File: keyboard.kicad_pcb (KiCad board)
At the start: 2 copper layers, 30 parts, among them J1 CONN-PALM-FOLD-KB, P1 CONN_25, P2 CONN_25, P3 PS2, P4 CONN_6, U1 CONN-X220-KB

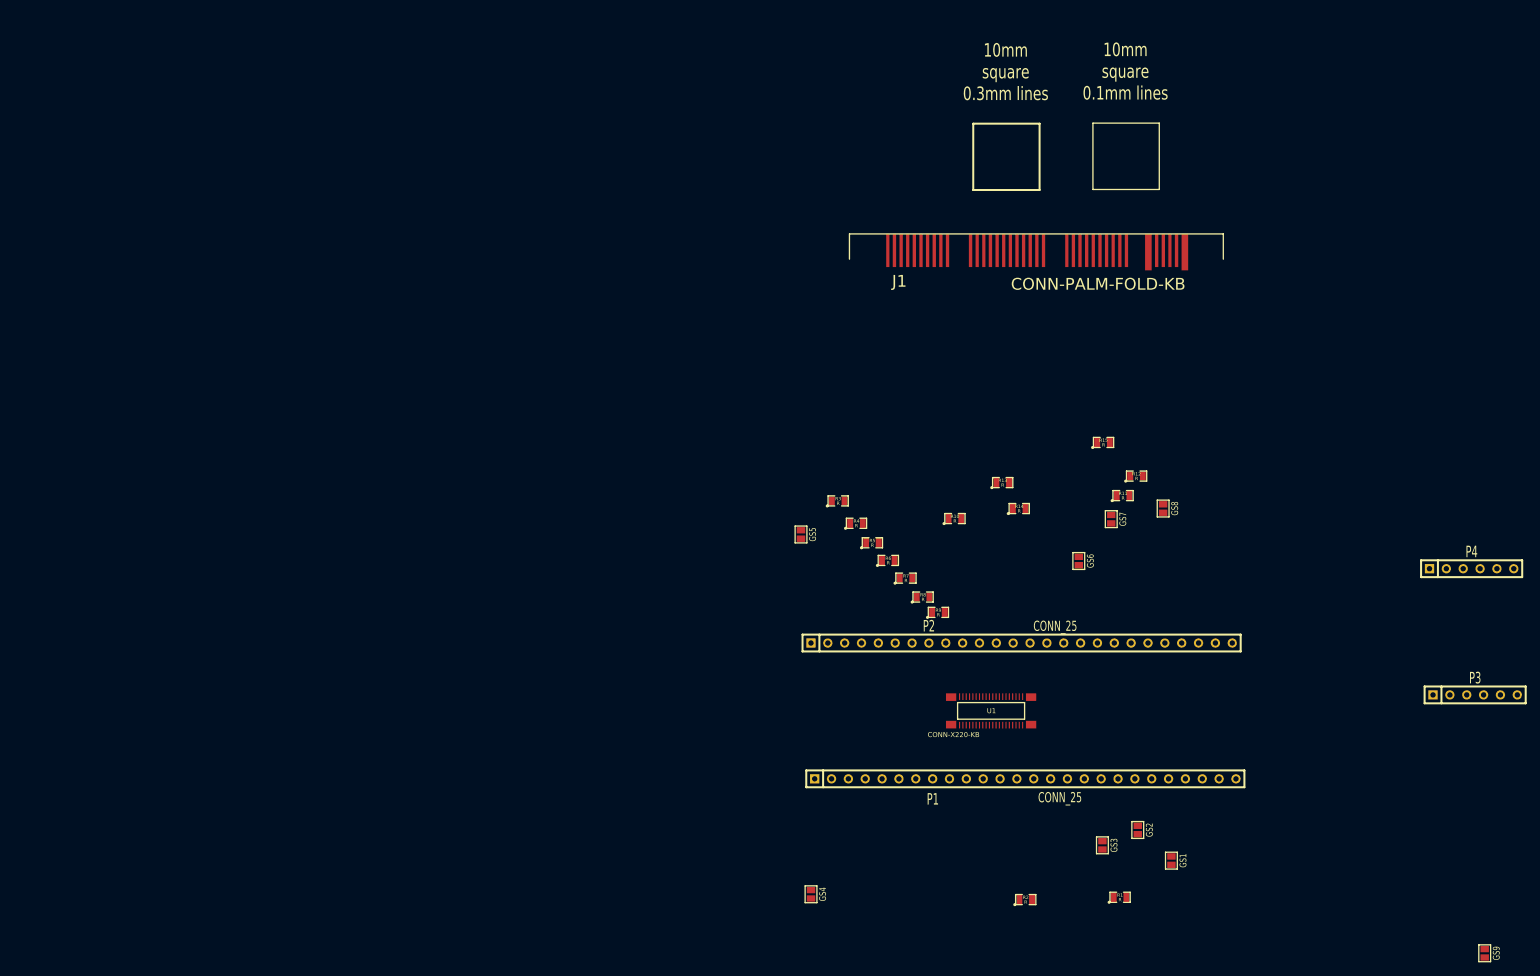
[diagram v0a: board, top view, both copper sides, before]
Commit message: Import all components into PCB
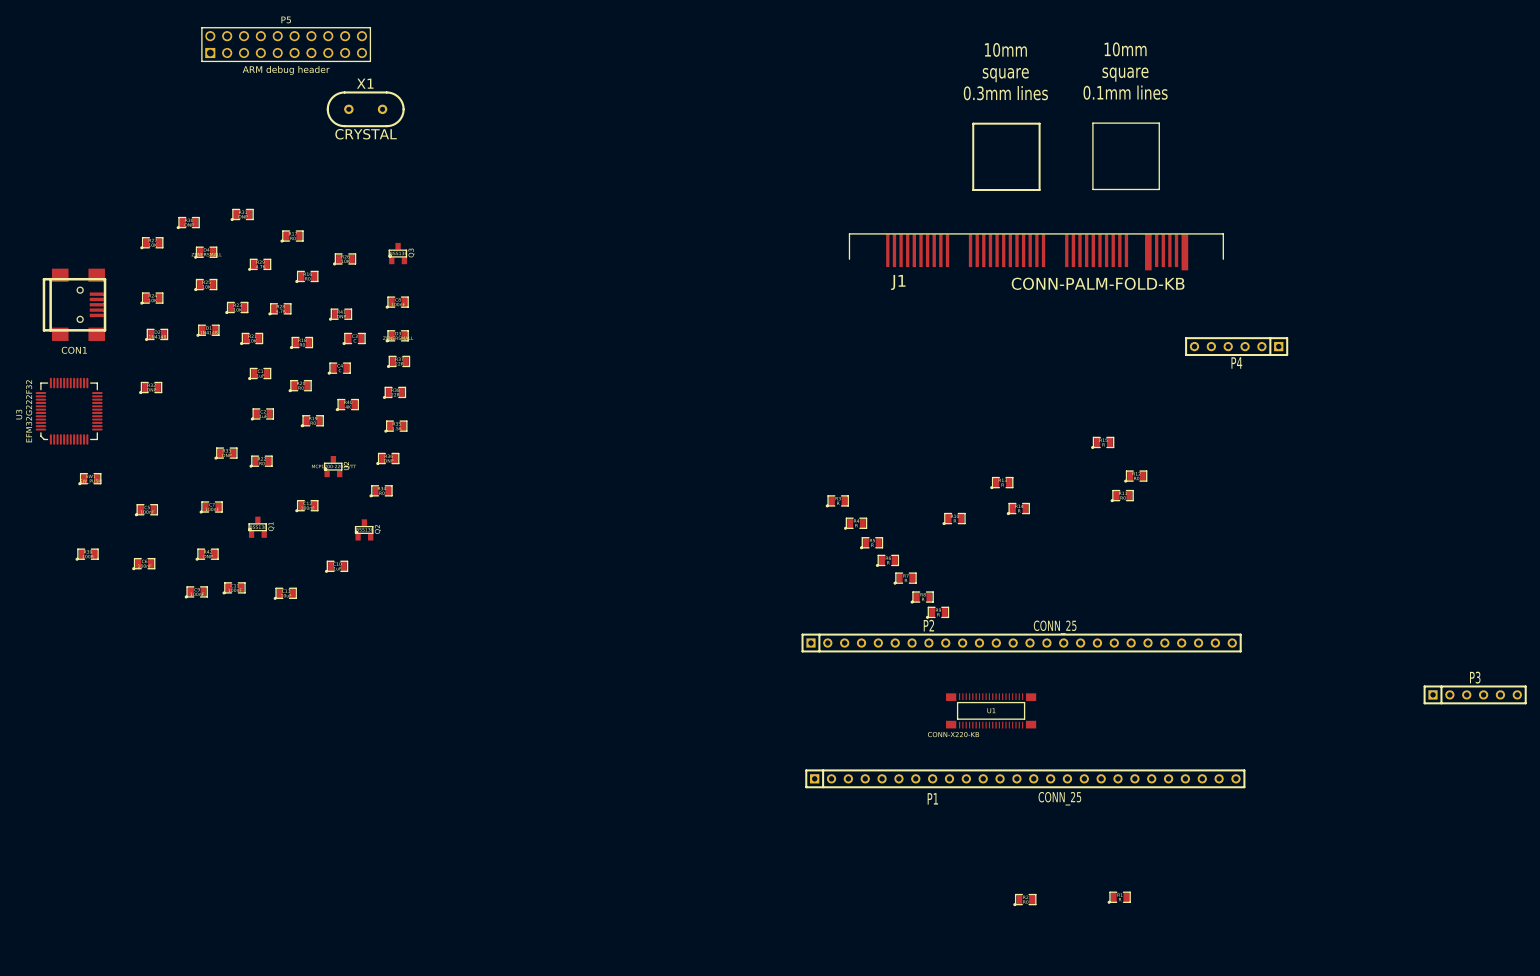
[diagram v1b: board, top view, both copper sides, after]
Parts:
- removed GS1, GS2, GS3, GS4, GS5, GS6, GS7, GS8, GS9: GS2, GS2
- added C1: 1uF, SM0805, F.Cu at (49.6, 67.7)
- added C10: 1uF, SM0805, F.Cu at (61.2, 96.7)
- added C11: 100nF, SM0805, F.Cu at (45.7, 100.0)
- added C12: 100nF, SM0805, F.Cu at (56.7, 87.6)
- added C13: 10uF, SM0805, F.Cu at (53.4, 100.8)
- added C2: 1uF, SM0805, F.Cu at (50.0, 73.8)
- added C3: C, SM0805, F.Cu at (63.8, 62.4)
- added C4: C, SM0805, F.Cu at (61.6, 66.8)
- added C5: 100nF, SM0805, F.Cu at (32.5, 88.2)
- added C6: 100nF, SM0805, F.Cu at (32.1, 96.3)
- added C7: 100nF, SM0805, F.Cu at (42.3, 87.8)
- added C8: 100nF, SM0805, F.Cu at (70.3, 56.9)
- added C9: 100nF, SM0805, F.Cu at (40.0, 100.6)
- added CON1: USB-MICRO-B, USB_MINI_B, F.Cu at (21.5, 57.3)
- added D1: 1N4148, SM0805, F.Cu at (41.8, 61.1)
- added D2: 1N4148, SM0805, F.Cu at (34.0, 61.8)
- added D3: ZENERSMALL, SM0805, F.Cu at (70.3, 62.0)
- added D4: ZENERSMALL, SM0805, F.Cu at (41.5, 49.4)
- added P5: ARM debug header, pin_array_10x2, F.Cu at (53.4, 18.1)
- added Q1: BSS138, SOT23, F.Cu at (49.2, 90.8)
- added Q2: BSS138, SOT23, F.Cu at (65.2, 91.2)
- added Q3: BSS138, SOT23, F.Cu at (70.3, 49.6)
- added R16: R0, SM0805, F.Cu at (56.7, 53.0)
- added R17: R0, SM0805, F.Cu at (54.5, 46.9)
- added R18: R0, SM0805, F.Cu at (55.9, 63.0)
- added R19: R0, SM0805, F.Cu at (57.5, 74.8)
- added R20: R0, SM0805, F.Cu at (55.7, 69.5)
- added R21: 10K, SM0805, F.Cu at (48.4, 62.4)
- added R22: R0, SM0805, F.Cu at (49.8, 80.9)
- added R23: 10K, SM0805, F.Cu at (46.1, 57.7)
- added R24: 10K, SM0805, F.Cu at (33.3, 56.3)
- added R25: 10K, SM0805, F.Cu at (41.5, 54.2)
- added R26: 10K, SM0805, F.Cu at (62.4, 50.4)
- added R27: 10K, SM0805, F.Cu at (33.3, 48.0)
- added R28: 4.7K, SM0805, F.Cu at (52.6, 57.9)
- added R29: 4.7K, SM0805, F.Cu at (49.6, 51.2)
- added R30: DNP, SM0805, F.Cu at (38.8, 44.9)
- added R31: DNP, SM0805, F.Cu at (46.9, 43.7)
- added R32: DNP, SM0805, F.Cu at (33.1, 69.8)
- added R33: DNP, SM0805, F.Cu at (44.5, 79.7)
- added R34: R0, SM0805, F.Cu at (67.9, 85.3)
- added R35: 1.5K, SM0805, F.Cu at (70.1, 75.6)
- added R36: DNP, SM0805, F.Cu at (68.9, 80.5)
- added R37: 22R, SM0805, F.Cu at (70.5, 65.8)
- added R38: 22R, SM0805, F.Cu at (69.9, 70.5)
- added R39: 100R, SM0805, F.Cu at (23.6, 94.9)
- added R40: 4K, SM0805, F.Cu at (62.8, 72.3)
- added R41: DNP, SM0805, F.Cu at (61.8, 58.7)
- added R42: DNP, SM0805, F.Cu at (41.7, 94.9)
- added SW1: SW_PUSH, SM0805, F.Cu at (24.0, 83.5)
- added U2: MCP1700-2202E/TT, SOT23, F.Cu at (60.6, 81.7)
- added U3: EFM32G222F32, EFM32_TQFP48, F.Cu at (20.7, 73.3)
- added X1: CRYSTAL, HC-49V, F.Cu at (65.4, 27.8)
- R11, R12, R2: value R -> R0
- moved P4 48.7 mm to (196.7, 63.6), turned to 180 degrees
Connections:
- P1 pad 18: N-0000020 (its old number) -> N-0000057
- P1 pad 20: N-0000018 (its old number) -> N-0000055
- P1 pad 22: N-0000016 (its old number) -> N-0000053
- R11 pad 2: tp4data -> N-0000055
- R12 pad 1: +5V -> GND
- R12 pad 2: tp4_clk -> N-0000057
- R13 pad 2: (no net) -> ledcpslock
- R14 pad 2: (no net) -> ledpwr
- R15 pad 2: (no net) -> led_mute
- R2 pad 1: +5V -> GND
- R2 pad 2: tp4_reset -> N-0000053
- U1 pad 34: N-0000020 (its old number) -> N-0000057
- U1 pad 38: N-0000018 (its old number) -> N-0000055
- U1 pad 44: N-0000016 (its old number) -> N-0000053

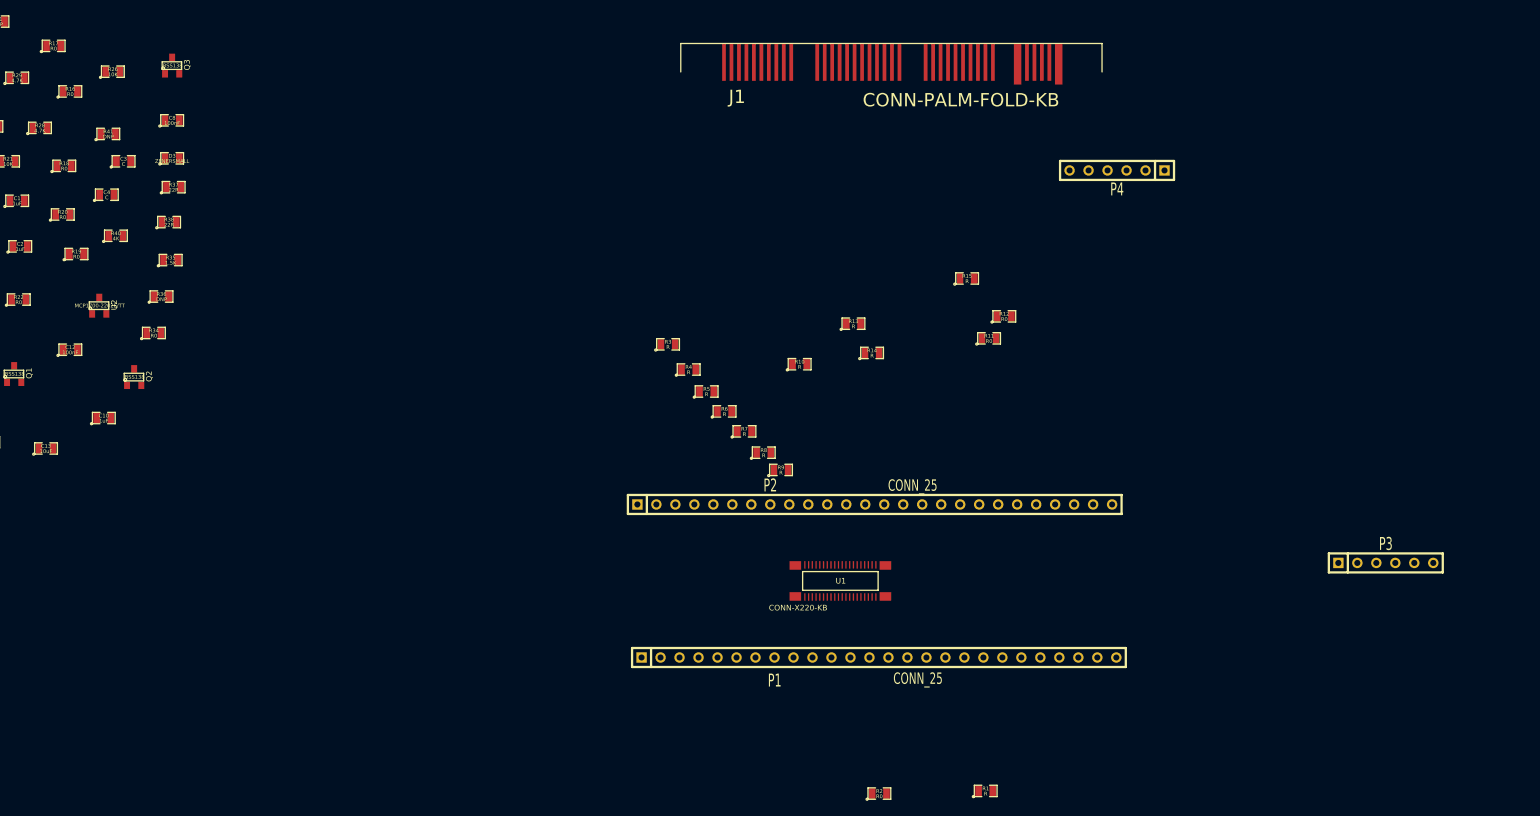
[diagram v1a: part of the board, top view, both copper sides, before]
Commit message: Give some components better labels, start playing around with initial part placement
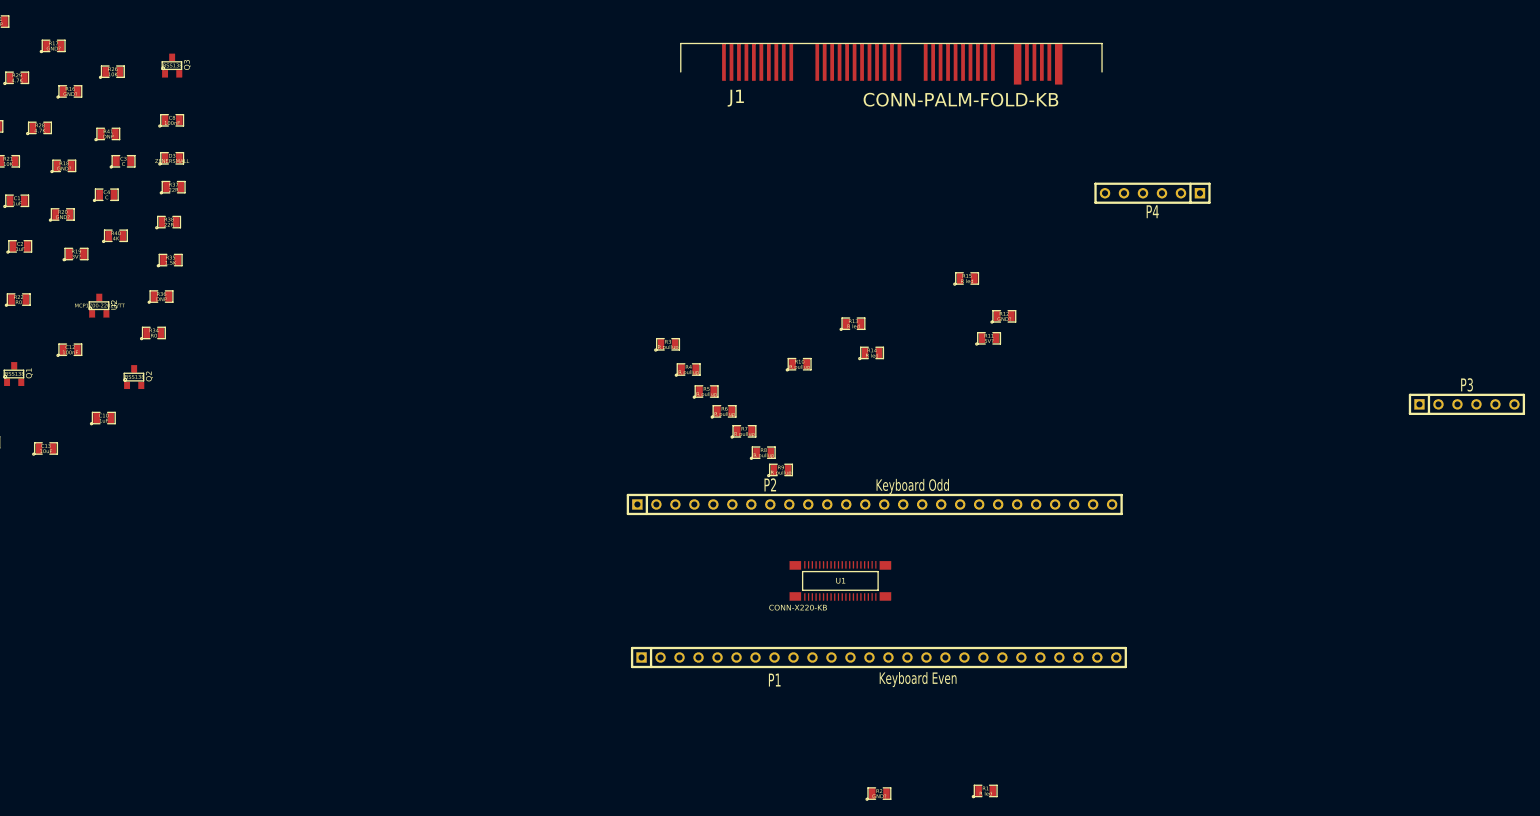
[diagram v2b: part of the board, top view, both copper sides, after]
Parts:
- P1: value CONN_25 -> Keyboard Even
- P2: value CONN_25 -> Keyboard Odd
- P4: value CONN_6 -> Palm Serial
- R1, R13, R14, R15: value R -> R led
- R10, R3, R4, R5, R6, R7, R8, R9: value R -> R pullup
- R11: value R0 -> 5V?
- R12, R16, R17, R18, R2, R20: value R0 -> GND?
- R19: value R0 -> 3V?
- moved P3 23.8 mm to (243.5, 94.9)
- moved P4 5.64 mm to (201.4, 66.7)

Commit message: Overlay the palm pcb footprint and start jamming parts into that shape
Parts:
- moved R24 232.6 mm to (265.3, 73.7)
- moved R21 231.3 mm to (274.5, 111.2)
- moved Q1 224.8 mm to (273.6, 103.8)
- moved R28 214.8 mm to (266.2, 80.4)
- moved Q2 208.6 mm to (273.6, 81.6)
- moved R29 202.0 mm to (250.7, 69.7)
- moved R26 183.1 mm to (244.9, 65.4)
- moved Q3 170.3 mm to (238.8, 74.6)
- moved U3 154.6 mm to (174.2, 54.7)
- moved CON1 149.6 mm to (169.6, 78.5), turned to 90 degrees
- moved R2 149.1 mm to (58.6, 42.4)
- moved D4 132.9 mm to (172.5, 71.5)
- moved X1 127.0 mm to (189.3, 56.0), turned to 90 degrees
- moved R11 125.3 mm to (56.4, 63.0)
- moved R12 125.3 mm to (58.5, 60.0)
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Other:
- net class Default: trace_width 0.2032 -> 0.254
- rule pad_to_mask_clearance: 0.254 -> 0
- rule trace_min: 0.2032 -> 0.254

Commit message: Attempt to interpret http://tinyurl.com/hvpcbfaq as kicad config
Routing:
- net col7: track 0.00 -> 28.5 mm, vias 0 -> 2
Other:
- net class Default: clearance 0.254 -> 0.15; trace_width 0.254 -> 0.15; via_dia 0.889 -> 0.6; via_drill 0.635 -> 0.3
- rule trace_clearance: 0.254 -> 0.15
- rule trace_min: 0.254 -> 0.15
- rule via_min_drill: 0.508 -> 0.3
- rule via_min_size: 0.889 -> 0.6
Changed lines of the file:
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@@
   (general
     (links 265)
-    (no_connects 265)
-    (area 12.3791 13.568 251.526401 148.142531)
+    (no_connects 264)
+    (area 30.172469 13.672 276.400439 147.688531)
     (thickness 1.6)
     (drawings 139)
-    (tracks 0)
+    (tracks 11)
     (zones 0)
     (modules 74)
@@
   )
   (setup
-    (last_trace_width 0.254)
-    (trace_clearance 0.254)
+    (last_trace_width 0.15)
+    (trace_clearance 0.15)
     (zone_clearance 0.508)
     (zone_45_only no)
-    (trace_min 0.254)
+    (trace_min 0.15)
     (segment_width 0.2)
     (edge_width 0.1)
-    (via_size 0.889)
-    (via_drill 0.635)
-    (via_min_size 0.889)
-    (via_min_drill 0.508)
+    (via_size 0.6)
+    (via_drill 0.3)
+    (via_min_size 0.6)
+    (via_min_drill 0.3)
     (uvia_size 0.508)
     (uvia_drill 0.127)
@@
   (net 75 tp4data)
   (net_class Default "This is the default net class."
-    (clearance 0.254)
-    (trace_width 0.254)
-    (via_dia 0.889)
-    (via_drill 0.635)
+    (clearance 0.15)
+    (trace_width 0.15)
+    (via_dia 0.6)
+    (via_drill 0.3)
     (uvia_dia 0.508)
     (uvia_drill 0.127)
@@
       (net 15 N-0000017)
     )
-    (model dil/dil_32-w600.wrl
-      (at (xyz 0 0 0))
-      (scale (xyz 1 1 1))
-      (rotate (xyz 0 0 0))
-    )
   )
   (module USB_MINI_B (layer F.Cu)
@@
   (gr_line (start 142.199998 43) (end 142.199998 48.800003) (angle 90) (layer F.SilkS) (width 0.127))
   (gr_line (start 199.1 43) (end 142.199998 43) (angle 90) (layer F.SilkS) (width 0.127))
+  (segment (start 148.03368 45.47428) (end 148.03368 48.41632) (width 0.15) (layer F.Cu) (net 54) (status 400000))
+  (segment (start 163.50228 48.37772) (end 163.50228 45.47428) (width 0.15) (layer F.Cu) (net 54) (status 800000))
+  (segment (start 163.49 48.39) (end 163.50228 48.37772) (width 0.15) (layer F.Cu) (net 54))
+  (via (at 163.49 48.39) (size 0.6) (layers F.Cu B.Cu) (net 54))
+  (segment (start 163.49 44.95) (end 163.49 48.39) (width 0.15) (layer B.Cu) (net 54))
+  (segment (start 162.91 44.37) (end 163.49 44.95) (width 0.15) (layer B.Cu) (net 54))
+  (segment (start 149.06 44.37) (end 162.91 44.37) (width 0.15) (layer B.Cu) (net 54))
+  (segment (start 148.03 45.4) (end 149.06 44.37) (width 0.15) (layer B.Cu) (net 54))
+  (segment (start 148.03 48.42) (end 148.03 45.4) (width 0.15) (layer B.Cu) (net 54))
+  (via (at 148.03 48.42) (size 0.6) (layers F.Cu B.Cu) (net 54))
+  (segment (start 148.03368 48.41632) (end 148.03 48.42) (width 0.15) (layer F.Cu) (net 54))
 )
